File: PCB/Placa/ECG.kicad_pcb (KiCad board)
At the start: 2 copper layers, 59.9 x 25.4 mm, 59 parts, among them P1 A_CONECTOR_DIN, P2 CONN_01X04, P3 CONN_01X04, P7 Shield, U1 INA333, U2 OPA2335, U3 OPA2335, U4 REF5050, U6 INA333, U7 OPA2335, U8 OPA2335, U9 OPA2335

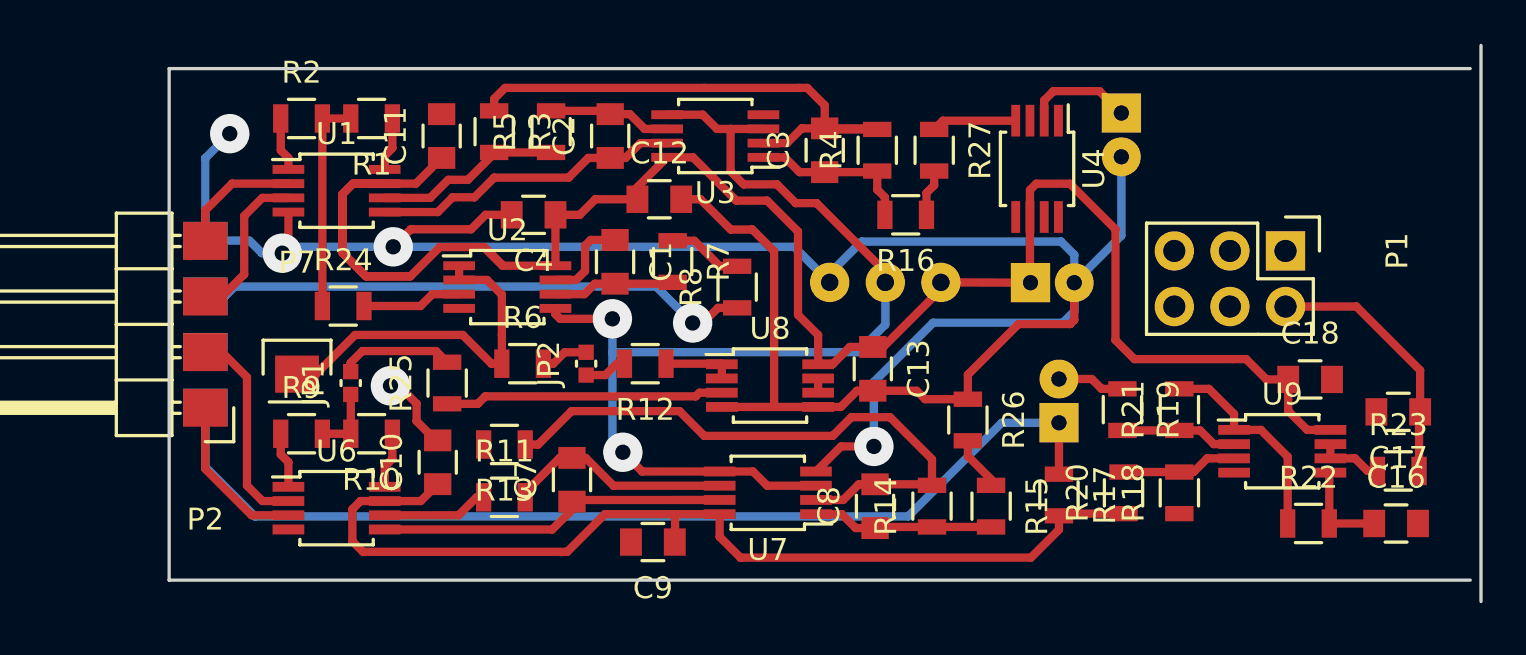
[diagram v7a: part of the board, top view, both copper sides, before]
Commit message: Terminé de rutear. Falta revisar si se puede mejorar
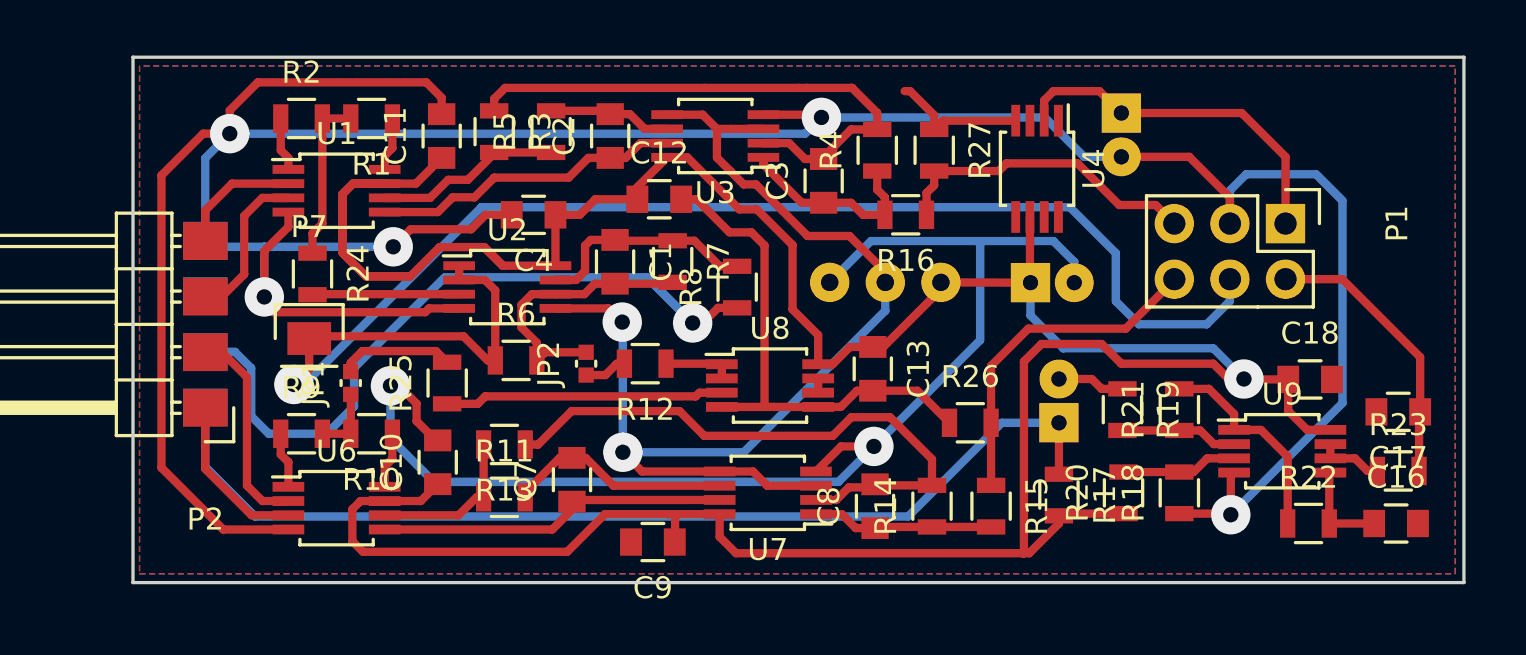
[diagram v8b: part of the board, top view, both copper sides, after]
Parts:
- moved R24 2.03 mm to (143.2, 80.5), turned to 270 degrees
- moved P7 1.72 mm to (143.1, 83.5)
- moved C3 1.40 mm to (166.6, 76.2)
- moved P1 1.25 mm to (187.7, 78.2)
- moved R6 0.34 mm to (152.5, 84.5)
- moved R26 0.17 mm to (173.2, 87.3), turned to 0 degrees
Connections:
- P1 pad 3: /Canales_ECG/SHIELD -> GND
- P1 pad 4: GND -> /Canales_ECG/SHIELD
- P3 pad 2: /Canales_ECG/RL -> (no net)
- P3 pad 3: (no net) -> /Canales_ECG/RL
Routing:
- net GND: track 122.2 -> 242.9 mm, vias 5 -> 7
- net /Canales_ECG/SHIELD: track 16.7 -> 68.1 mm, vias 0 -> 1
- net +5V: track 135.1 -> 148.9 mm, vias 0 -> 1
- net /Canales_ECG/OUT_ch2: track 2.47 -> 15.5 mm
- net /Canales_ECG/OUT_ch1: track 4.16 -> 15.9 mm
- net +BATT: track 5.04 -> 16.4 mm
- net /Canales_ECG/RL: track 25.5 -> 35.2 mm
- net /Canales_ECG/filtro: track 7.74 -> 12.6 mm
- net Net-(C1-Pad1): track 7.59 -> 10.2 mm
- net Net-(R11-Pad1): track 4.86 -> 7.27 mm
- net Net-(R1-Pad2): track 9.87 -> 7.64 mm
- net Net-(R24-Pad2): track 4.58 -> 6.71 mm
- net Net-(C3-Pad1): track 9.11 -> 10.8 mm
- net /Canales_ECG/REF: track 50.1 -> 51.4 mm
- net /Microfono/OUT_Mic: track 11.9 -> 12.8 mm
- added copper zone on B.Cu, net (none)
- added copper zone on F.Cu, net GND
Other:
- board size 59.9 x 25.4 mm -> 60.8 x 24 mm
